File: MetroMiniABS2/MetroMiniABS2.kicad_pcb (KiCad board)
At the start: 2 copper layers, 80 x 64.8 mm, 40 parts, among them CON1 PJ_037A, IC1 MCT6H, J1 RJ45, J2 RJ45, P1 Termination, P2 + 12V (IN) -, P3 In Track Out, P4 +5 G Y R GND, P5 - 12V (out) +, SW1 Blue, SW2 Gold, U1 METROMINI, U2 MCP2517, U3 MCP2551, X1 20 Mhz

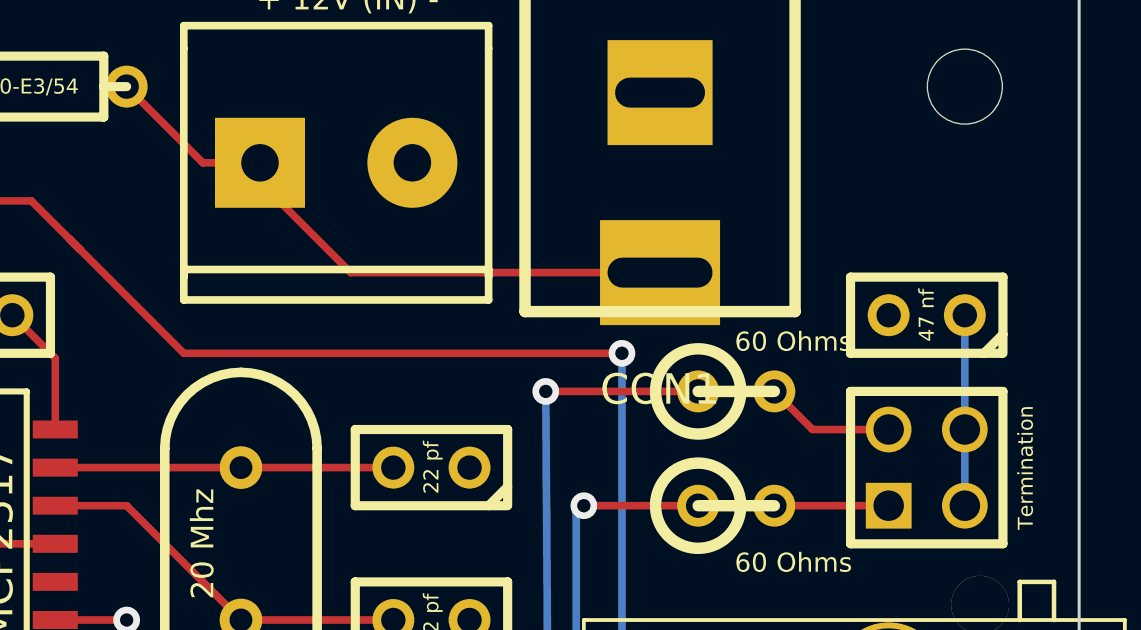
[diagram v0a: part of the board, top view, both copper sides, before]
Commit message: Add power jumper.
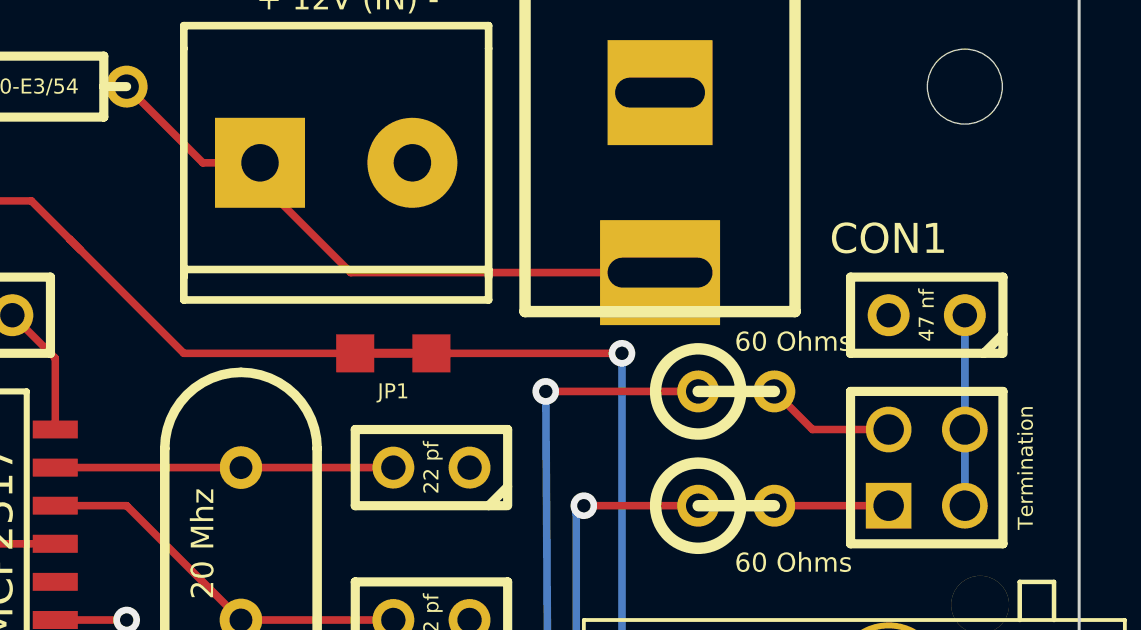
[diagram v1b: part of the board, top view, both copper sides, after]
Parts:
- added JP1: JUMPER, ClosedJumper, F.Cu at (141.0, 115.6)
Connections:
- D1 pad 1: N-0000020 (its old number) -> N-0000021
- D2 pad 2: N-0000020 (its old number) -> N-0000021
- J1 pad 8: N-0000020 (its old number) -> N-000001
- J2 pad 8: N-0000020 (its old number) -> N-000001
- P5 pad 1: N-0000020 (its old number) -> N-0000021
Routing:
- net N-0000020 (its old number): track 73.1 -> 0.00 mm, vias 3 -> 0
- net N-000001: track 0.00 -> 47.8 mm, vias 0 -> 3
- net N-0000021: track 0.00 -> 22.7 mm
